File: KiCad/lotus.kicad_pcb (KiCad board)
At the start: 2 copper layers, 32 parts, among them IC1 DW01A-G, J1 USB_OTG, J2 FTDI, Q1 FS8205A, SW1 SW_Push, SW2 SW_DIP_x01, SW3 SW_Push, U1 LD1117S33CTR, U2 TP4056, U3 ESP-12E

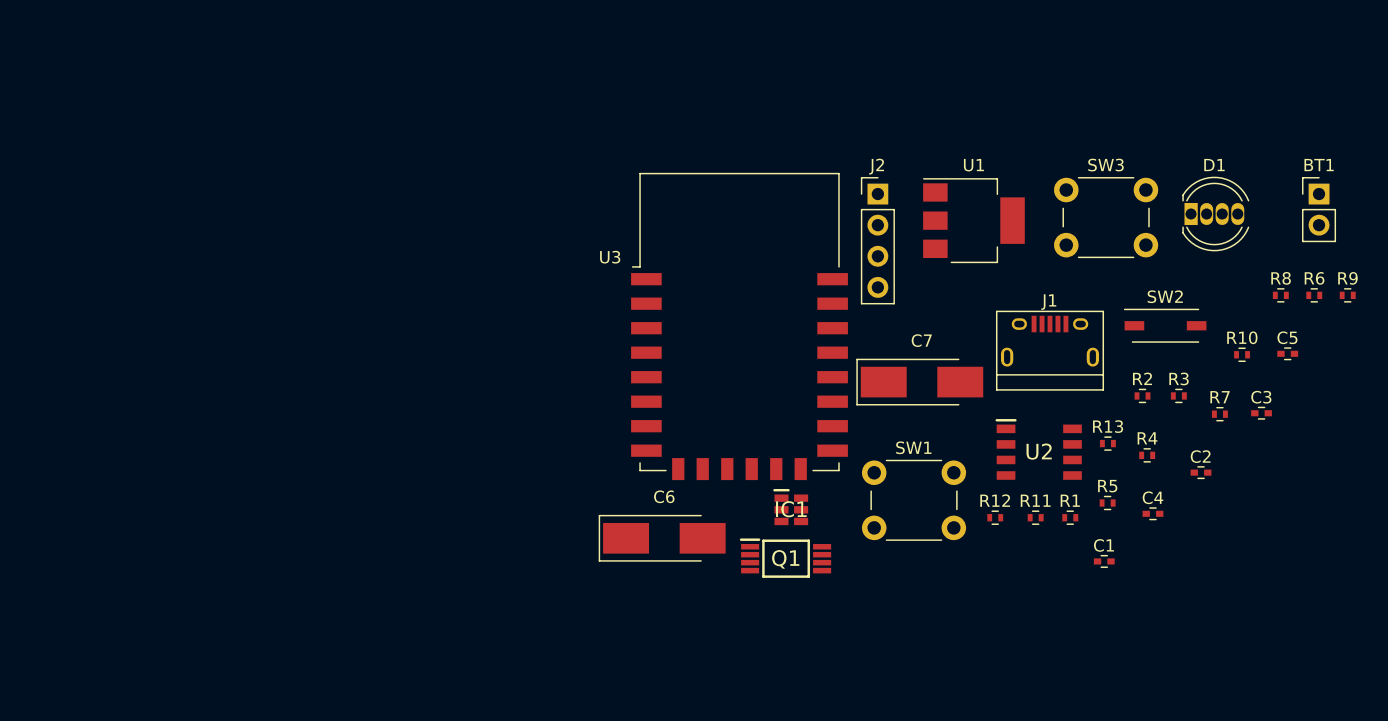
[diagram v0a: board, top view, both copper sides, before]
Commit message: Organizado footprints no PCB
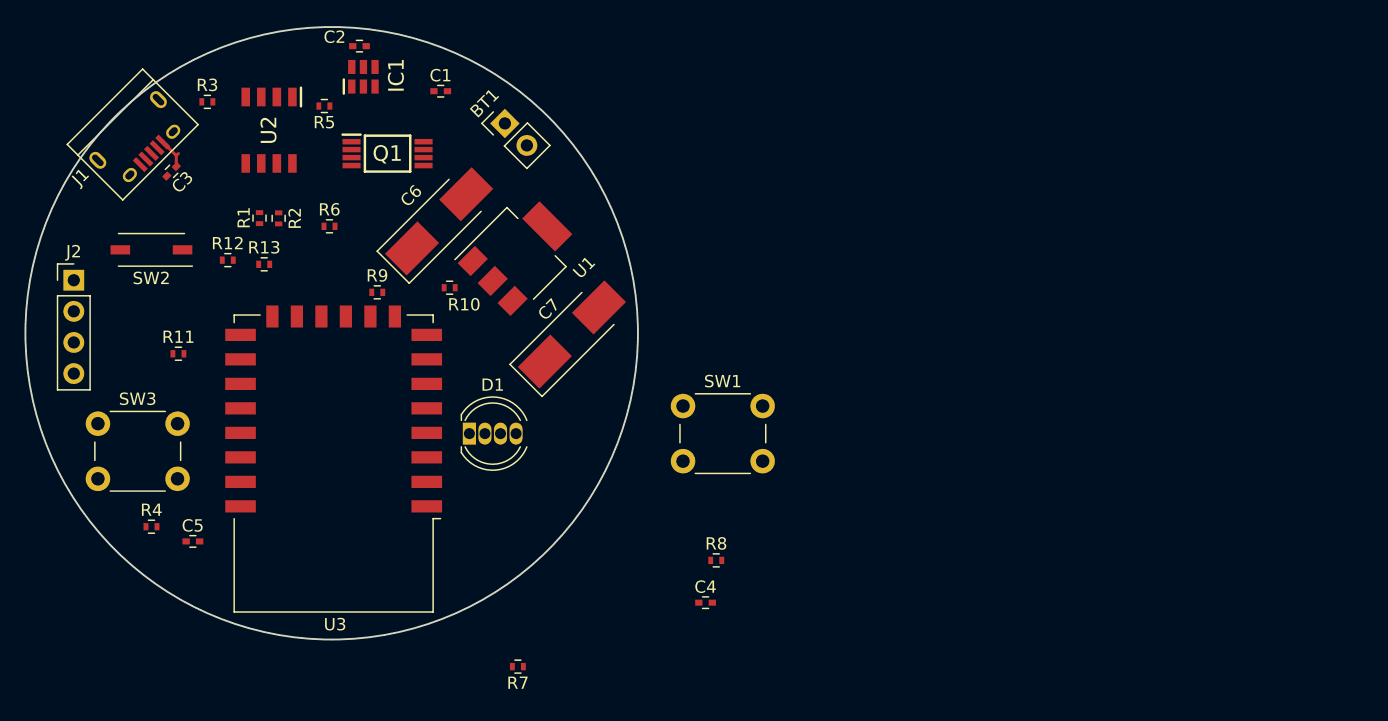
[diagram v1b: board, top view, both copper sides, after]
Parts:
- moved C3 91.1 mm to (141.9, 101.8), turned to 225 degrees
- moved C5 90.7 mm to (143.7, 132.0)
- moved SW2 83.0 mm to (140.3, 108.2), turned to 180 degrees
- moved R3 82.9 mm to (144.8, 96.1)
- moved R4 81.5 mm to (140.3, 130.8)
- moved SW3 81.3 mm to (135.9, 122.4)
- moved R6 80.6 mm to (154.8, 106.3)
- moved R9 79.2 mm to (158.7, 111.7)
- moved C2 77.0 mm to (157.3, 91.6)
- moved J1 76.0 mm to (139.3, 99.4), turned to 225 degrees
- moved R2 72.0 mm to (150.7, 105.6), turned to 270 degrees
- moved R5 71.7 mm to (154.4, 96.5), turned to 180 degrees
- moved R11 71.2 mm to (142.5, 116.7)
- moved R1 70.6 mm to (149.1, 105.6), turned to 270 degrees
- moved R13 70.4 mm to (149.5, 109.4)
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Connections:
- R10 pad 1: Net-(R10-Pad1) -> VCC
- R11 pad 2: Net-(R10-Pad1) -> VCC
- R12 pad 1: Net-(R12-Pad1) -> VCC
- R12 pad 2: pin_chrg -> pin_stdby
- R13 pad 1: Net-(R12-Pad1) -> VCC
- R13 pad 2: pin_stdby -> pin_chrg
- U3 pad 13: pin_stdby -> pin_chrg
- U3 pad 14: pin_chrg -> pin_stdby
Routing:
- net Net-(C3-Pad1): track 0.00 -> 2.69 mm
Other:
- board outline added: 50 x 50 mm
